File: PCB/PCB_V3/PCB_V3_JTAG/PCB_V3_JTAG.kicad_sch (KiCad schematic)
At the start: 76 parts, among them J1 ESP_Left, J10 MCP_RIGHT, J11 ACS2_pins, J12 ACS4_Pins, J13 ACS2_Screw, J14 ACS4_Screw, J15 MCP_VCC_LINE, J16 AMS_IP_Pins, J17 AMS_OP_Pins, J18 BC1_IN+, J19 BC1_IN-, J2 ESP_Right, J20 BC3_IN+, J21 BC3_IN-, J22 BC1_OUT+, J23 BC1_OUT-, J24 BC3_OUT+, J25 BC3_OUT-, J26 BC2_IN+, J27 BC2_IN-, J28 BC5_IN+, J29 BC5_IN-, J3 ACS1_Pins, J30 BC2_OUT+, J31 BC2_OUT-, J32 BC5_OUT+, J33 BC5_OUT-, J34 LED_LHS_JTAG, J35 LED_RHS_JTAG, J4 ACS3_Pins, J44 STATIC_LED_1, J45 STATIC_LED_2, J46 I/P_Terminal, J47 Battery_Terminal, J5 ACS3_Screw, J6 ACS1_Screw, J7 LAN_Pins_2, J8 MCP_LEFT, J9 LAN_Pins_1, Q1 IRLZ44N, Q10 IRLZ44N, Q2 IRLZ44N, Q3 IRLZ44N, Q4 IRLZ44N, Q5 IRLZ44N, Q6 IRLZ44N, Q7 IRLZ44N, Q8 IRLZ44N, Q9 IRLZ44N

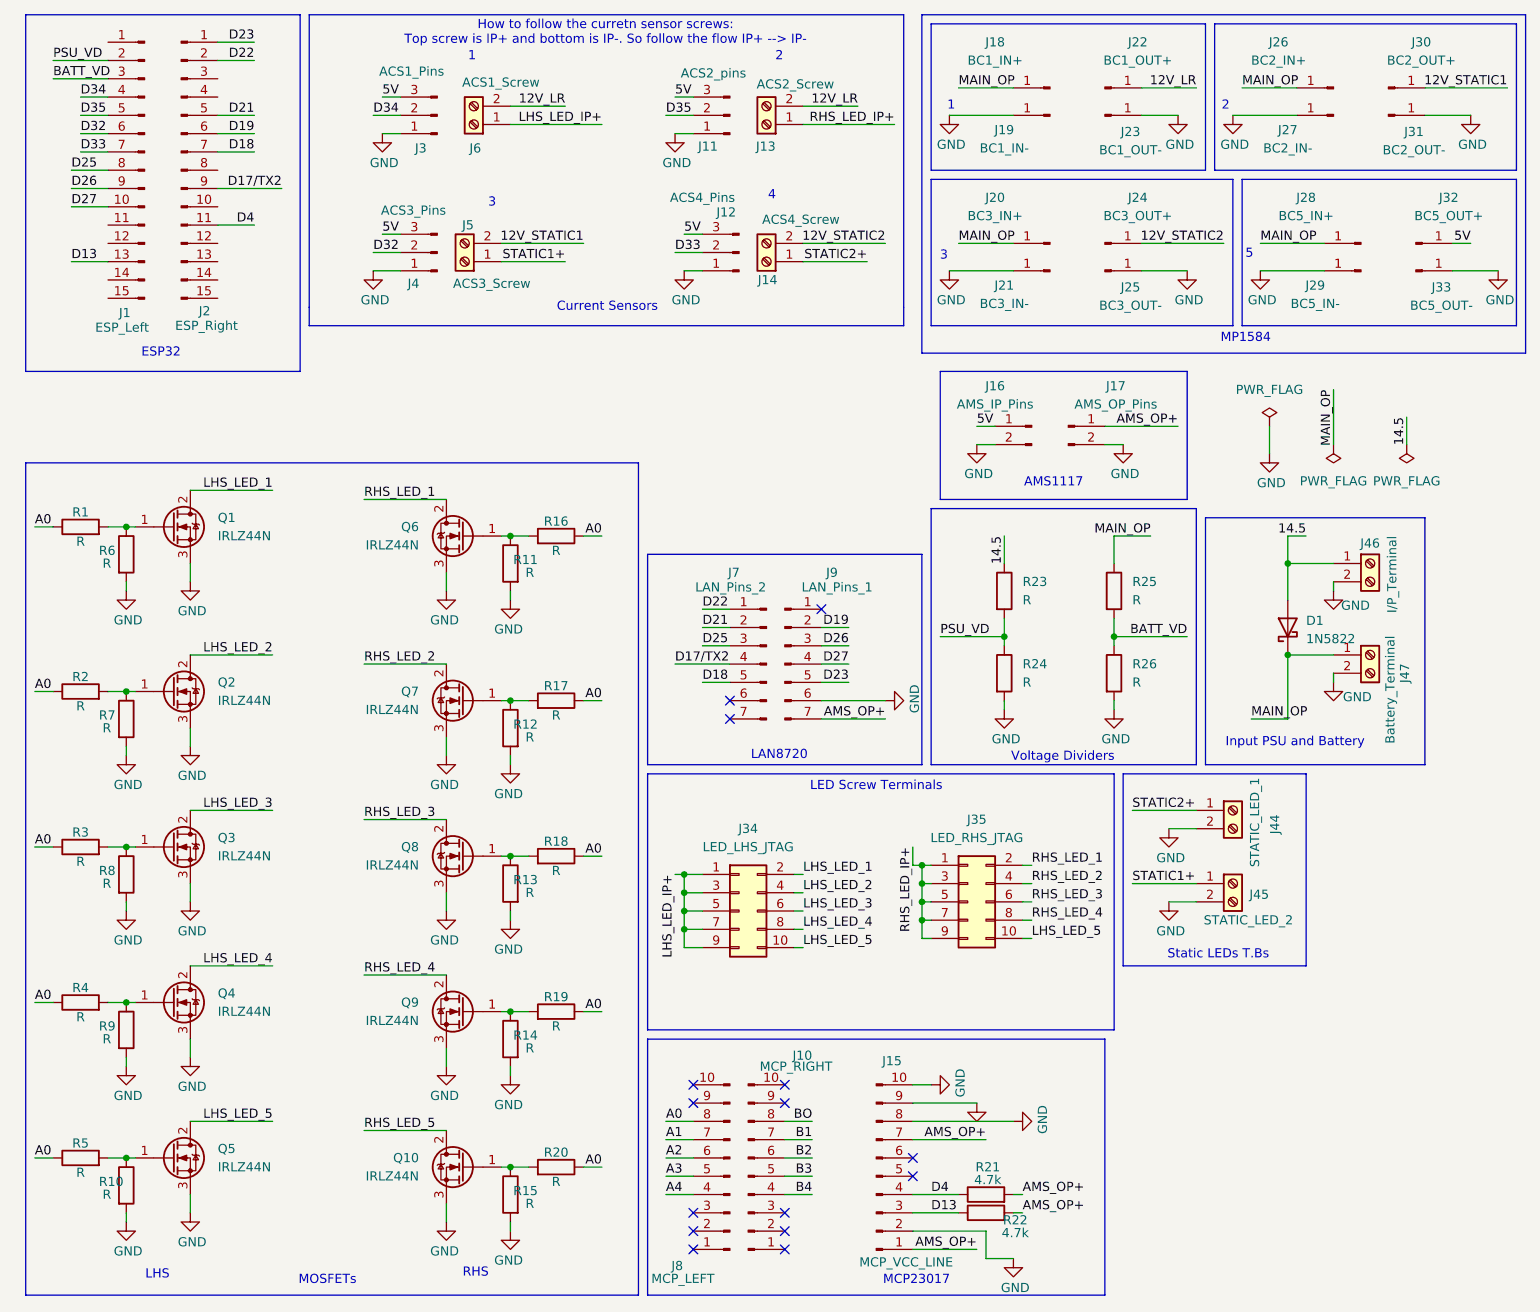
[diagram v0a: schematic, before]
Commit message: corrected a fe thing sin the schematic file
1. Some of the MCP outputs were wrongly marked, so corrected that
2. B0 and BO were incorrectly marked, corrected that
3. Assigned the appropriate footprint for the JTAG pins
4. changed the MCp from 2 induvidual pins for A0 B0, to a single 02x10 connector
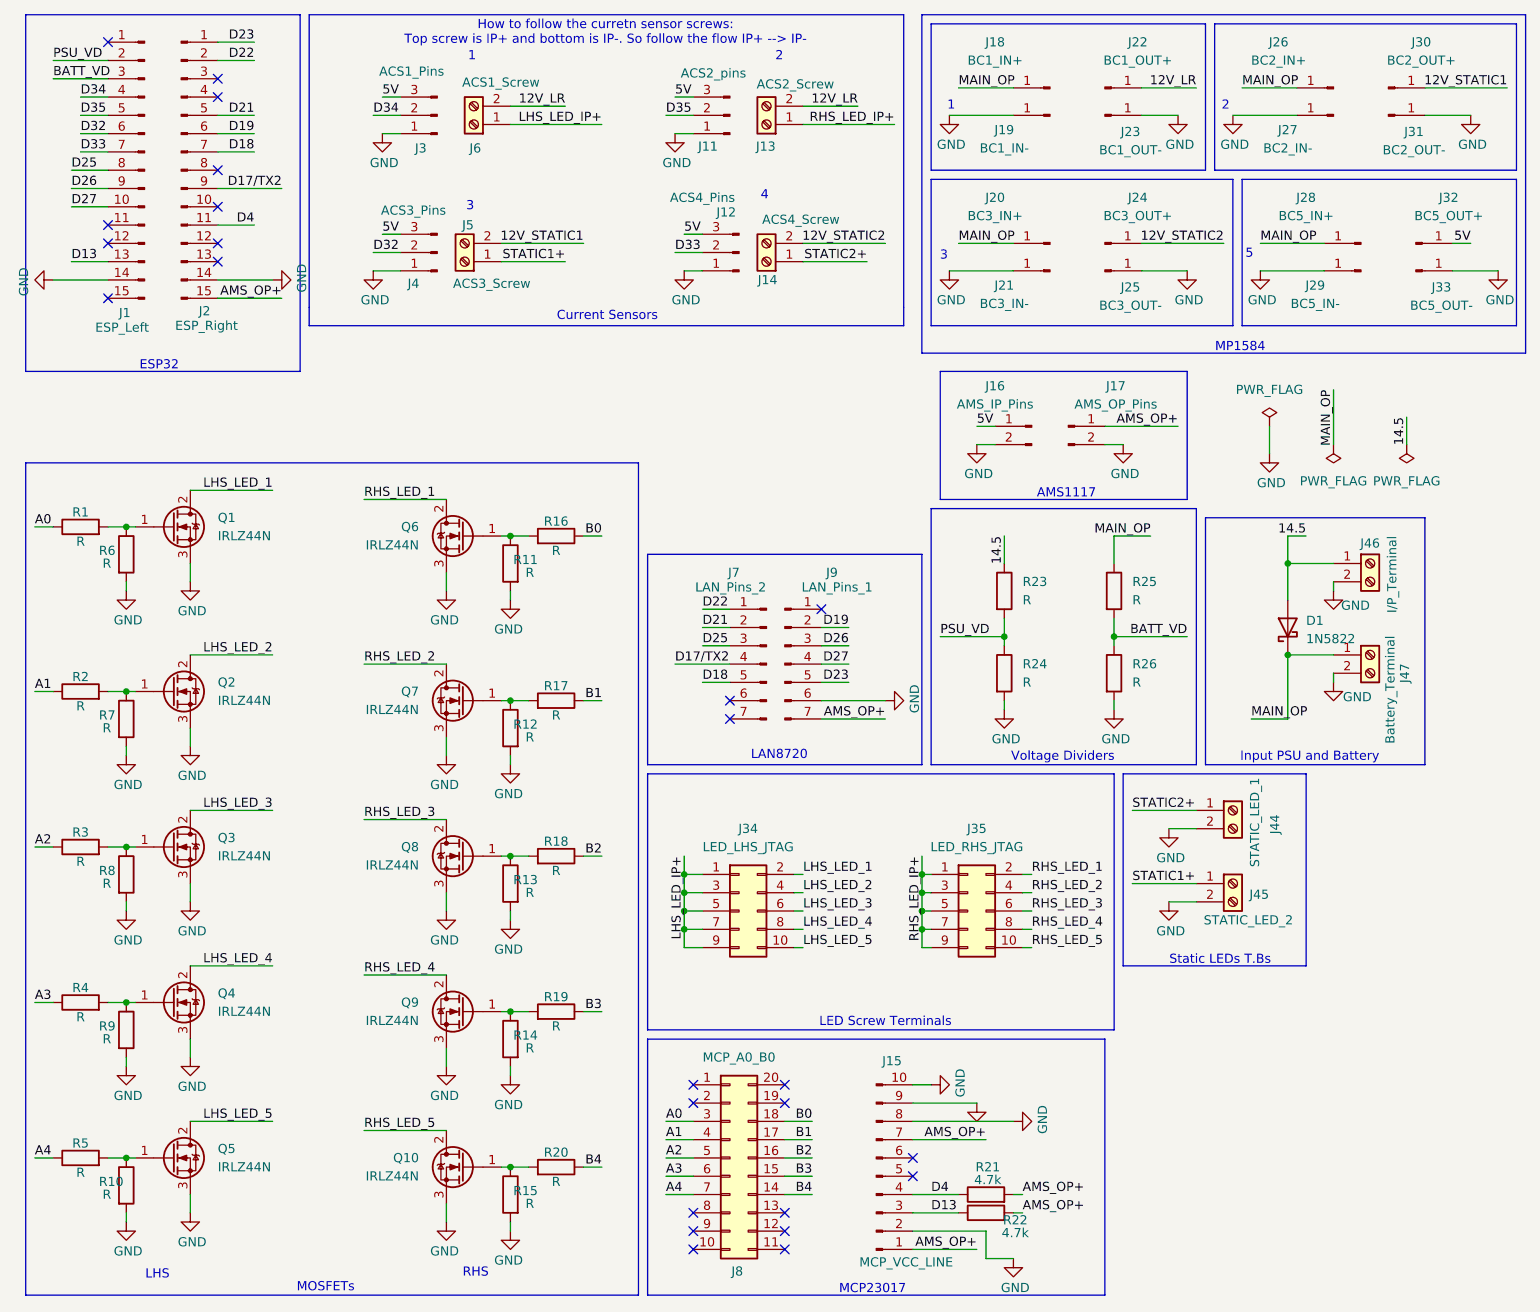
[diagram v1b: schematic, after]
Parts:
- removed J10: MCP_RIGHT, Connector_PinHeader_2.54mm:PinHeader_1x10_P2.54mm_Vertical, symbol Connector:Conn_01x10_Pin
- removed J8: MCP_LEFT, Connector_PinHeader_2.54mm:PinHeader_1x10_P2.54mm_Vertical, symbol Connector:Conn_01x10_Pin
- added J8: MCP_A0_B0, Connector_PinSocket_2.54mm:PinSocket_2x10_P2.54mm_Vertical, symbol Connector_Generic:Conn_02x10_Counter_Clockwise
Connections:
- net A0: now also J8.3 (Pin_3); no longer R16.1, R17.1, R18.1, R19.1, R2.1, R20.1, R3.1, R4.1, R5.1
- net A1: now also R2.1, J8.4 (Pin_4)
- net A2: now also R3.1, J8.5 (Pin_5)
- net A3: now also R4.1, J8.6 (Pin_6)
- net A4: now also R5.1, J8.7 (Pin_7)
- net AMS_OP+: now also J2.15 (Pin_15)
- net B1: now also R17.1, J8.17 (Pin_17)
- net B2: now also R18.1, J8.16 (Pin_16)
- net B3: now also R19.1, J8.15 (Pin_15)
- net B4: now also R20.1, J8.14 (Pin_14)
- net GND: now also J1.14 (Pin_14), J2.14 (Pin_14)
- net LHS_LED_5: no longer J35.10 (Pin_10)
- net RHS_LED_5: now also J35.10 (Pin_10)
- new net B0: J8.18 (Pin_18), R16.1
- no-connect marks 15 -> 25
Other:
- moved on the sheet: J35

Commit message: Updated the schematic and fixed the PCB viewer 3D models
1. Schematic finalization
2. PCB 3D models, berg stick removal
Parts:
- removed J7: LAN_Pins_2, Connector_PinHeader_2.54mm:PinHeader_1x07_P2.54mm_Vertical, symbol Connector:Conn_01x07_Pin
- removed J9: LAN_Pins_1, Connector_PinHeader_2.54mm:PinHeader_1x07_P2.54mm_Vertical, symbol Connector:Conn_01x07_Pin
- added J7: Conn_02x07_Counter_Clockwise, Connector_PinSocket_2.54mm:PinSocket_2x07_P2.54mm_Vertical, symbol Connector_Generic:Conn_02x07_Counter_Clockwise
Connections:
- net AMS_OP+: now also J7.8 (Pin_8)
- net D17/TX2: now also J7.4 (Pin_4)
- net D18: now also J7.5 (Pin_5)
- net D19: now also J7.13 (Pin_13)
- net D21: now also J7.2 (Pin_2)
- net D22: now also J7.1 (Pin_1)
- net D23: now also J7.10 (Pin_10)
- net D25: now also J7.3 (Pin_3)
- net D26: now also J7.12 (Pin_12)
- net D27: now also J7.11 (Pin_11)
- net GND: now also J7.9 (Pin_9)
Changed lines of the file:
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@@
 	)
 	(symbol
-		(lib_id "Connector:Conn_01x07_Pin")
-		(at 120.65 105.41 0)
-		(unit 1)
-		(body_style 1)
-		(exclude_from_sim no)
-		(in_bom yes)
-		(on_board yes)
-		(in_pos_files yes)
-		(dnp no)
-		(property "Reference" "J9"
-			(at 128.016 92.71 0)
-			(show_name no)
-			(do_not_autoplace no)
-			(effects
-				(font
-					(size 1.27 1.27)
-				)
-				(justify right)
-			)
-		)
-		(property "Value" "LAN_Pins_1"
-			(at 132.842 94.742 0)
-			(show_name no)
-			(do_not_autoplace no)
-			(effects
-				(font
-					(size 1.27 1.27)
-				)
-				(justify right)
-			)
-		)
-		(property "Footprint" "Connector_PinHeader_2.54mm:PinHeader_1x07_P2.54mm_Vertical"
-			(at 120.65 105.41 0)
-			(hide yes)
-			(show_name no)
-			(do_not_autoplace no)
-			(effects
-				(font
-					(size 1.27 1.27)
-				)
-			)
-		)
-		(property "Datasheet" ""
-			(at 120.65 105.41 0)
-			(hide yes)
-			(show_name no)
-			(do_not_autoplace no)
-			(effects
-				(font
-					(size 1.27 1.27)
-				)
-			)
-		)
-		(property "Description" "Generic connector, single row, 01x07, script generated"
-			(at 120.65 105.41 0)
-			(hide yes)
-			(show_name no)
-			(do_not_autoplace no)
-			(effects
-				(font
-					(size 1.27 1.27)
-				)
-			)
-		)
-		(pin "3"
-		)
-		(pin "7"
-		)
-		(pin "1"
-		)
-		(pin "2"
-		)
-		(pin "6"
-		)
-		(pin "5"
-		)
-		(pin "4"
-		)
-		(instances
-			(project "PCB_V3_JTAG"
-				(path "/ee241afc-090c-4762-b5af-0318d3704def"
-					(reference "J9")
-					(unit 1)
-				)
-			)
-		)
-	)
-	(symbol
 		(lib_id "power:GND")
 		(at 82.55 162.56 0)
@@
 	)
 	(symbol
-		(lib_id "Connector:Screw_Terminal_01x02")
-		(at 201.93 104.14 0)
+		(lib_id "Connector_Generic:Conn_02x07_Counter_Clockwise")
+		(at 118.11 105.41 0)
 		(unit 1)
 		(body_style 1)
@@
 		(in_pos_files yes)
 		(dnp no)
-		(property "Reference" "J47"
-			(at 206.756 106.68 90)
+		(fields_autoplaced yes)
+		(property "Reference" "J7"
+			(at 119.38 91.44 0)
 			(show_name no)
 			(do_not_autoplace no)
@@
 			)
 		)
-		(property "Value" "Battery_Terminal"
-			(at 204.724 108.966 90)
+		(property "Value" "Conn_02x07_Counter_Clockwise"
+			(at 119.38 93.98 0)
 			(show_name no)
 			(do_not_autoplace no)
@@
 			)
 		)
-		(property "Footprint" "TerminalBlock_Phoenix:TerminalBlock_Phoenix_MKDS-1,5-2-5.08_1x02_P5.08mm_Horizontal"
-			(at 201.93 104.14 0)
+		(property "Footprint" "Connector_PinSocket_2.54mm:PinSocket_2x07_P2.54mm_Vertical"
+			(at 118.11 105.41 0)
 			(hide yes)
 			(show_name no)
@@
 		)
 		(property "Datasheet" ""
-			(at 201.93 104.14 0)
+			(at 118.11 105.41 0)
 			(hide yes)
 			(show_name no)
@@
 			)
 		)
-		(property "Description" "Generic screw terminal, single row, 01x02, script generated (kicad-library-utils/schlib/autogen/connector/)"
-			(at 201.93 104.14 0)
+		(property "Description" "Generic connector, double row, 02x07, counter clockwise pin numbering scheme (similar to DIP package numbering), script generated (kicad-library-utils/schlib/autogen/connector/)"
+			(at 118.11 105.41 0)
 			(hide yes)
 			(show_name no)
@@
 		(pin "1"
 		)
+		(pin "3"
+		)
+		(pin "4"
+		)
+		(pin "6"
+		)
+		(pin "5"
+		)
+		(pin "8"
+		)
+		(pin "7"
+		)
+		(pin "14"
+		)
+		(pin "13"
+		)
+		(pin "12"
+		)
+		(pin "11"
+		)
+		(pin "10"
+		)
+		(pin "9"
+		)
 		(instances
 			(project "PCB_V3_JTAG"
 				(path "/ee241afc-090c-4762-b5af-0318d3704def"
-					(reference "J47")
+					(reference "J7")
 					(unit 1)
 				)
@@
 	)
 	(symbol
-		(lib_id "Connector:Conn_01x07_Pin")
-		(at 118.11 105.41 0)
-		(mirror y)
+		(lib_id "Connector:Screw_Terminal_01x02")
+		(at 201.93 104.14 0)
 		(unit 1)
 		(body_style 1)
@@
 		(in_pos_files yes)
 		(dnp no)
-		(property "Reference" "J7"
-			(at 112.776 92.71 0)
+		(property "Reference" "J47"
+			(at 206.756 106.68 90)
 			(show_name no)
 			(do_not_autoplace no)
@@
 					(size 1.27 1.27)
 				)
-				(justify right)
 			)
 		)
-		(property "Value" "LAN_Pins_2"
-			(at 108.204 94.742 0)
+		(property "Value" "Battery_Terminal"
+			(at 204.724 108.966 90)
 			(show_name no)
 			(do_not_autoplace no)
@@
 					(size 1.27 1.27)
 				)
-				(justify right)
 			)
 		)
-		(property "Footprint" "Connector_PinHeader_2.54mm:PinHeader_1x07_P2.54mm_Vertical"
-			(at 118.11 105.41 0)
+		(property "Footprint" "TerminalBlock_Phoenix:TerminalBlock_Phoenix_MKDS-1,5-2-5.08_1x02_P5.08mm_Horizontal"
+			(at 201.93 104.14 0)
 			(hide yes)
 			(show_name no)
@@
 		)
 		(property "Datasheet" ""
-			(at 118.11 105.41 0)
+			(at 201.93 104.14 0)
 			(hide yes)
 			(show_name no)
@@
 			)
 		)
-		(property "Description" "Generic connector, single row, 01x07, script generated"
-			(at 118.11 105.41 0)
+		(property "Description" "Generic screw terminal, single row, 01x02, script generated (kicad-library-utils/schlib/autogen/connector/)"
+			(at 201.93 104.14 0)
 			(hide yes)
 			(show_name no)
@@
 			)
 		)
-		(pin "3"
-		)
-		(pin "7"
-		)
-		(pin "1"
-		)
 		(pin "2"
 		)
-		(pin "6"
-		)
-		(pin "5"
-		)
-		(pin "4"
+		(pin "1"
 		)
 		(instances
 			(project "PCB_V3_JTAG"
 				(path "/ee241afc-090c-4762-b5af-0318d3704def"
-					(reference "J7")
+					(reference "J47")
 					(unit 1)
 				)

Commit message: misc.
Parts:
- removed J34: LED_LHS_JTAG, Connector_PinSocket_2.54mm:PinSocket_2x05_P2.54mm_Vertical, symbol Connector_Generic:Conn_02x05_Odd_Even
- removed J35: LED_RHS_JTAG, Connector_PinSocket_2.54mm:PinSocket_2x05_P2.54mm_Vertical, symbol Connector_Generic:Conn_02x05_Odd_Even
- removed J7: Conn_02x07_Counter_Clockwise, Connector_PinSocket_2.54mm:PinSocket_2x07_P2.54mm_Vertical, symbol Connector_Generic:Conn_02x07_Counter_Clockwise
- removed J8: MCP_A0_B0, Connector_PinSocket_2.54mm:PinSocket_2x10_P2.54mm_Vertical, symbol Connector_Generic:Conn_02x10_Counter_Clockwise
- added J10: LHS_Arrow_+ve, Connector_PinSocket_2.54mm:PinSocket_1x05_P2.54mm_Vertical, symbol Connector:Conn_01x05_Pin
- added J34: LHS_Arrow_-ve, Connector_PinSocket_2.54mm:PinSocket_1x05_P2.54mm_Vertical, symbol Connector:Conn_01x05_Pin
- added J35: RHS_Arrow_-ve, Connector_PinSocket_2.54mm:PinSocket_1x05_P2.54mm_Vertical, symbol Connector:Conn_01x05_Pin
- added J36: RHS_Arrow_+ve, Connector_PinSocket_2.54mm:PinSocket_1x05_P2.54mm_Vertical, symbol Connector:Conn_01x05_Pin
- added J37: LAN8720_pins_1, Connector_PinSocket_2.54mm:PinSocket_1x07_P2.54mm_Vertical, symbol Connector:Conn_01x07_Pin
- added J7: LAN8720_pins_2, Connector_PinSocket_2.54mm:PinSocket_1x07_P2.54mm_Vertical, symbol Connector:Conn_01x07_Pin
- added J8: MCP_B0, Connector_PinSocket_2.54mm:PinSocket_1x10_P2.54mm_Vertical, symbol Connector:Conn_01x10_Pin
- added J9: MCP_A0, Connector_PinSocket_2.54mm:PinSocket_1x10_P2.54mm_Vertical, symbol Connector:Conn_01x10_Pin
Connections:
- net A0: now also J9.3 (Pin_3)
- net A1: now also J9.4 (Pin_4)
- net A2: now also J9.5 (Pin_5)
- net A3: now also J9.6 (Pin_6)
- net A4: now also J9.7 (Pin_7)
- net AMS_OP+: now also J37.7 (Pin_7)
- net B0: now also J8.3 (Pin_3)
- net B1: now also J8.4 (Pin_4)
- net B2: now also J8.5 (Pin_5)
- net B3: now also J8.6 (Pin_6)
- net B4: now also J8.7 (Pin_7)
- net D17/TX2: now also J7.4 (Pin_4)
- net D18: now also J7.5 (Pin_5)
- net D19: now also J37.2 (Pin_2)
- net D21: now also J7.2 (Pin_2)
- net D22: now also J7.1 (Pin_1)
- net D23: now also J37.5 (Pin_5)
- net D25: now also J7.3 (Pin_3)
- net D26: now also J37.3 (Pin_3)
- net D27: now also J37.4 (Pin_4)
- net GND: now also J37.6 (Pin_6)
- net LHS_LED_1: now also J34.1 (Pin_1)
- net LHS_LED_2: now also J34.2 (Pin_2)
- net LHS_LED_3: now also J34.3 (Pin_3)
- net LHS_LED_4: now also J34.4 (Pin_4)
- net LHS_LED_5: now also J34.5 (Pin_5)
- net LHS_LED_IP+: now also J10.1 (Pin_1), J10.2 (Pin_2), J10.3 (Pin_3), J10.4 (Pin_4), J10.5 (Pin_5)
- net RHS_LED_1: now also J35.1 (Pin_1)
- net RHS_LED_2: now also J35.2 (Pin_2)
- net RHS_LED_3: now also J35.3 (Pin_3)
- net RHS_LED_4: now also J35.4 (Pin_4)
- net RHS_LED_5: now also J35.5 (Pin_5)
- net RHS_LED_IP+: now also J36.1 (Pin_1), J36.2 (Pin_2), J36.3 (Pin_3), J36.4 (Pin_4), J36.5 (Pin_5)
